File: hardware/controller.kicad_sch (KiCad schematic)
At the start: 47 parts, among them J1 Connector, USB-TYPE-C-16P, U1 ESP32-C6-WROOM-1, U2 BQ24074RGTR, U3 TLA2518IRTER, U4 CH343P, U6 TPS62142RGTR, X1 12MHz

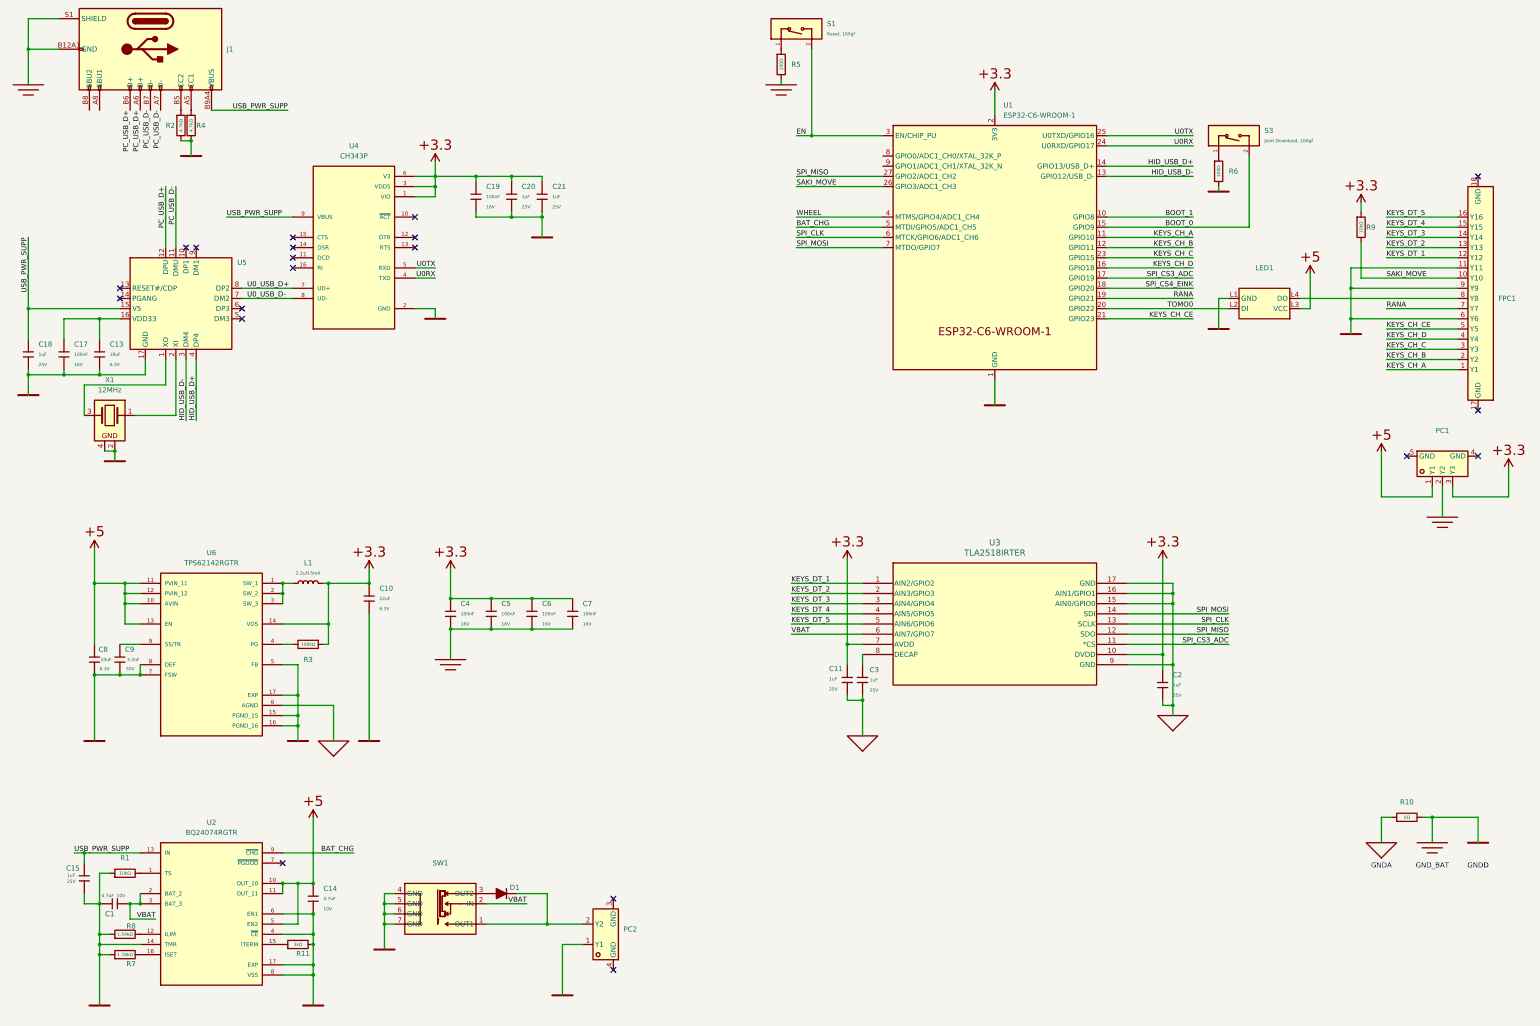
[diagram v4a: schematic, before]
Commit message: :sparkles: finish pcb layout of controller
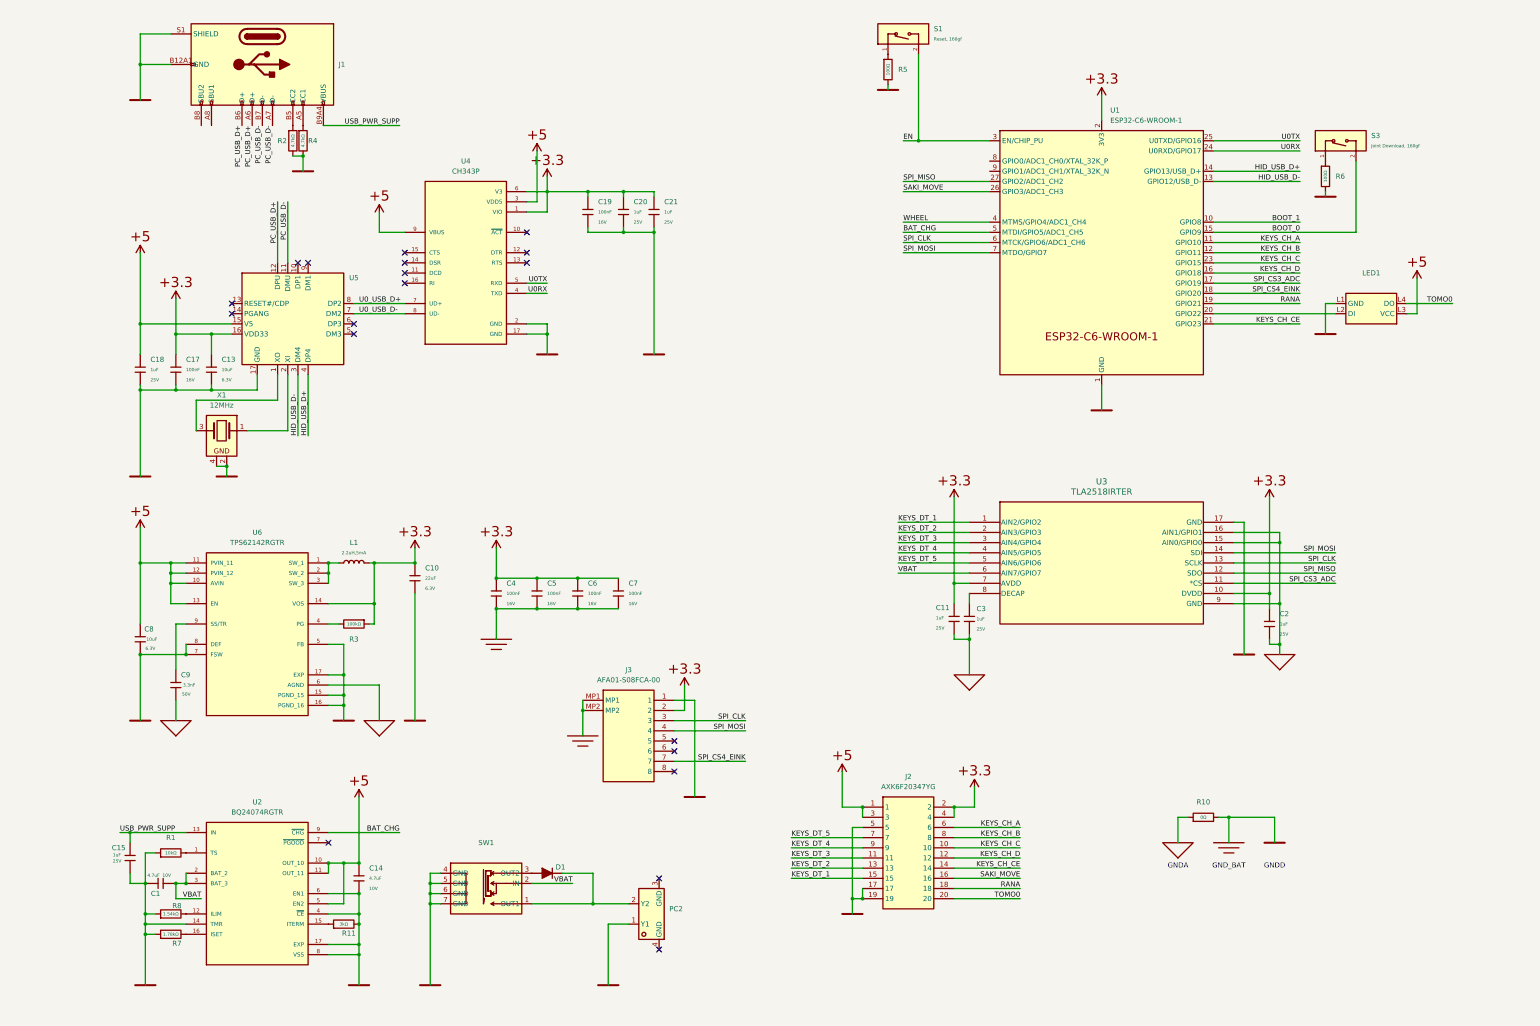
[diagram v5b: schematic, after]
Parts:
- removed FPC1: ~, KeysDock:AFC01-S16FCA-00, symbol components:FPC-SMD_AFC01-S16FCA
- removed PC1: ~, KeysDock:ZX-ZH1.5-3PWT, symbol components:ZX-ZH1.5-3PWT
- removed R9: 10kΩ, KeysDock:R_0402, symbol components:0402,10kΩ
- added J2: AXK6F20347YG, KeysDock:AXK6F20347YG, symbol components:AXK6F20347YG
- added J3: AFA01-S08FCA-00, KeysDock:AFA01-S08FCA-00, symbol components:AFA01-S08FCA-00
- X1: footprint PCM_Crystal_AKL:Crystal_SMD_3225-4Pin_3.2x2.5mm -> KeysDock:Crystal_SMD_3225-4P
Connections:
- net GND is gone; now on net P,E: U4.17 (GND)
- net P,0 is gone; now on net P,E: X1.2, X1.4
- net KEYS_CH_A: now also J2.6
- net KEYS_CH_B: now also J2.8
- net KEYS_CH_C: now also J2.10
- net KEYS_CH_CE: now also J2.14
- net KEYS_CH_D: now also J2.12
- net KEYS_DT_1: now also J2.15
- net KEYS_DT_2: now also J2.13
- net KEYS_DT_3: now also J2.11
- net KEYS_DT_4: now also J2.9
- net KEYS_DT_5: now also J2.7
- net P,+3.3: now also C13.1, C17.1, U5.16 (VDD33), J2.2, J2.4, J3.2; no longer U4.3 (VDD5)
- net P,+5: now also C18.1, U4.3 (VDD5), U4.9 (VBUS), U5.15 (V5), J2.1, J2.3
- net P,E: now also U3.17 (GND), J2.17, J2.19, J2.5, J3.1, J3.MP1, J3.MP2; no longer C9.2
- net P,GND: now also C9.2; no longer U3.17 (GND)
- net RANA: now also J2.18
- net SAKI_MOVE: now also J2.16
- net SPI_CLK: now also J3.3
- net SPI_CS4_EINK: now also J3.7
- net SPI_MOSI: now also J3.4
- net TOMO0: now also LED1.L4 (DO), J2.20; no longer LED1.L2 (DI), U1.20 (GPIO22)
- net USB_PWR_SUPP: no longer C18.1, U4.9 (VBUS), U5.15 (V5)
- new net: LED1.L2 (DI), U1.20 (GPIO22)
- no-connect marks 20 -> 19
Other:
- moved on the sheet: C1, C10, C11, C13, C14, C15, C17, C18, C19, C2, C20, C21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

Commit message: :fire: remove CH-series chips and use legacy UART
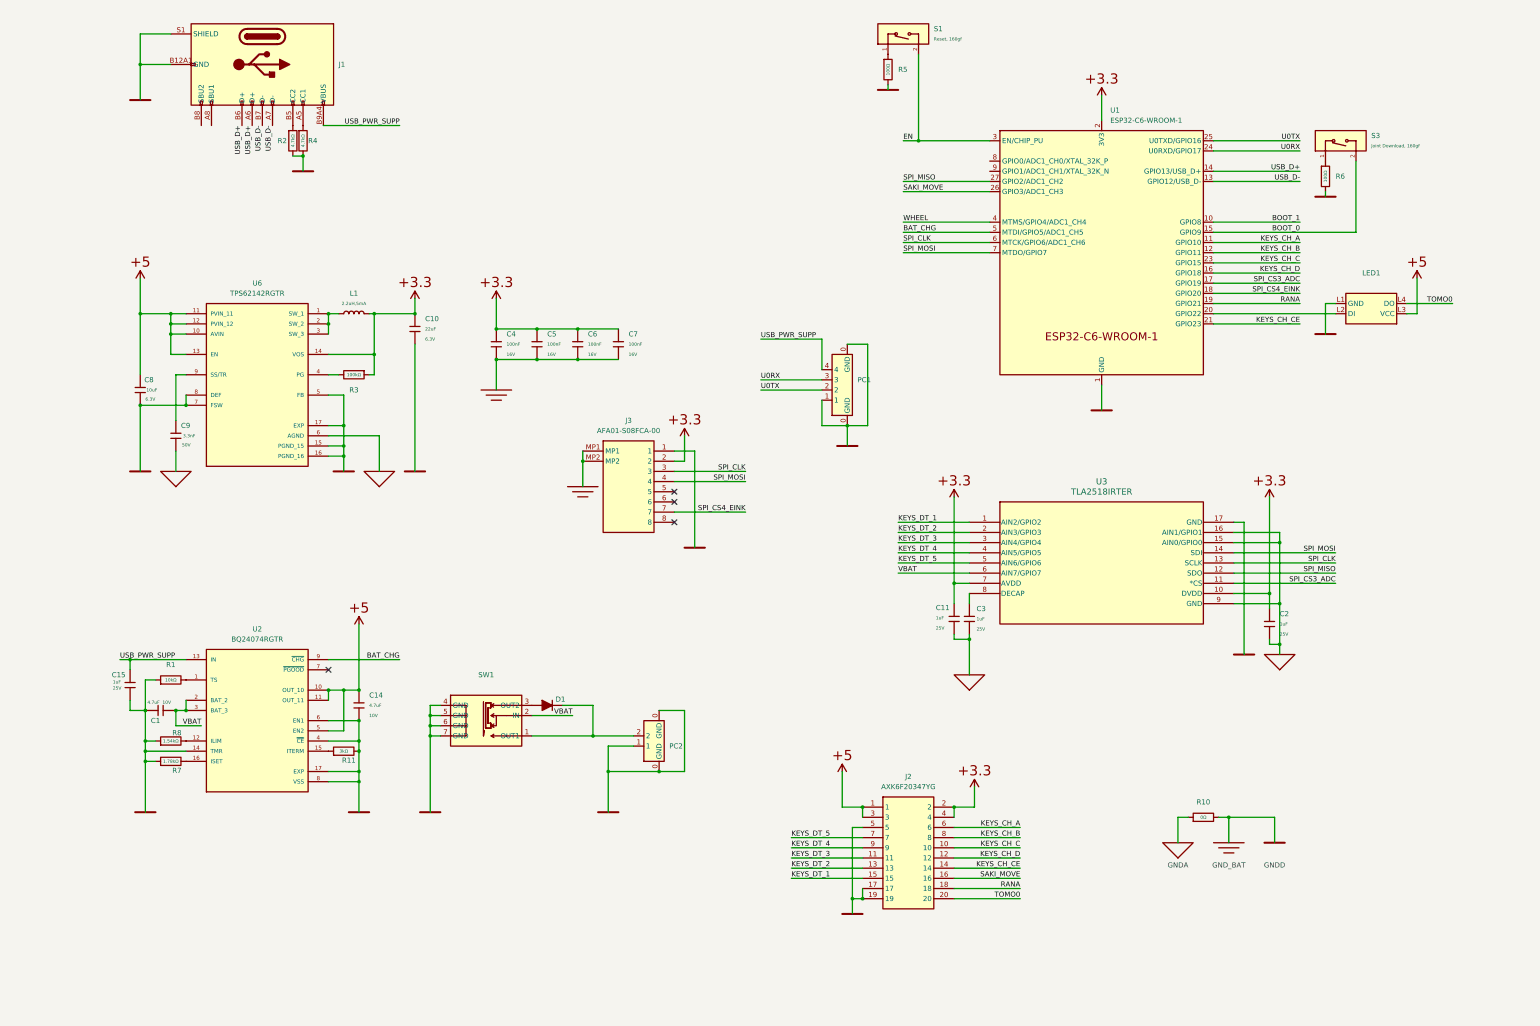
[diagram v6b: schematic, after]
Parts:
- removed C13: 10uF, KeysDock:C_0402, symbol components:0402,10uF
- removed C17, C19: 100nF, KeysDock:C_0402, symbol components:0402,100nF
- removed C18, C20, C21: 1uF, KeysDock:C_0402, symbol components:0402,1uF
- removed U4: CH343P, KeysDock:QFN50P300X300X80-17N, symbol components:CH343P
- removed U5: ~, KeysDock:QFN50P300X300X80-17N, symbol components:CH334P
- removed X1: 12MHz, KeysDock:Crystal_SMD_3225-4P, symbol components:YXC-YSO110TR
- added PC1: ~, KeysDock:HC-1.25-4PWT, symbol components:HC-1.25-4PWT
- PC2: footprint KeysDock:ZX-ZH1.5-2PWT -> KeysDock:HC-1.25-2PWT; symbol components:ZX-ZH1.5-2PWT -> components:HC-1.25-2PWT
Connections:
- net PC_USB_D+ is gone; now on net USB_D+: J1.A6 (D+), J1.B6 (D+)
- net PC_USB_D- is gone; now on net USB_D-: J1.A7 (D-), J1.B7 (D-)
- net P,E: now also PC2.0 (GND), PC1.0 (GND), PC1.1
- net U0RX: now also PC1.3
- net U0TX: now also PC1.2
- net USB_PWR_SUPP: now also PC1.4
- net HID_USB_D+ renamed USB_D+
- net HID_USB_D- renamed USB_D-
- no-connect marks 19 -> 4
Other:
- moved on the sheet: C1, C10, C14, C15, C4, C5, C6, C7, C8, C9, D1, J3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
